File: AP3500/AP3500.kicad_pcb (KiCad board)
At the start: 4 copper layers, 105 x 105 mm, 146 parts, among them IC2 TPS23751PWPR, J1 Console, J11 Barrel_Jack, J12 Bus_PCI_Express_Mini, J9 0826-1X1T-GH-F, Q1 FDS86242, U1 TPD4EUSB30, U10 TPS563249DDCR, U11 TPS563249DDCR, U12 HMHA2801AR2, U13 TPS563249DDCR, U2 TPD4EUSB30, U3 SN74LVC07AD, U5 74LVC1G07SE-7, U6 TL431AIDBVR

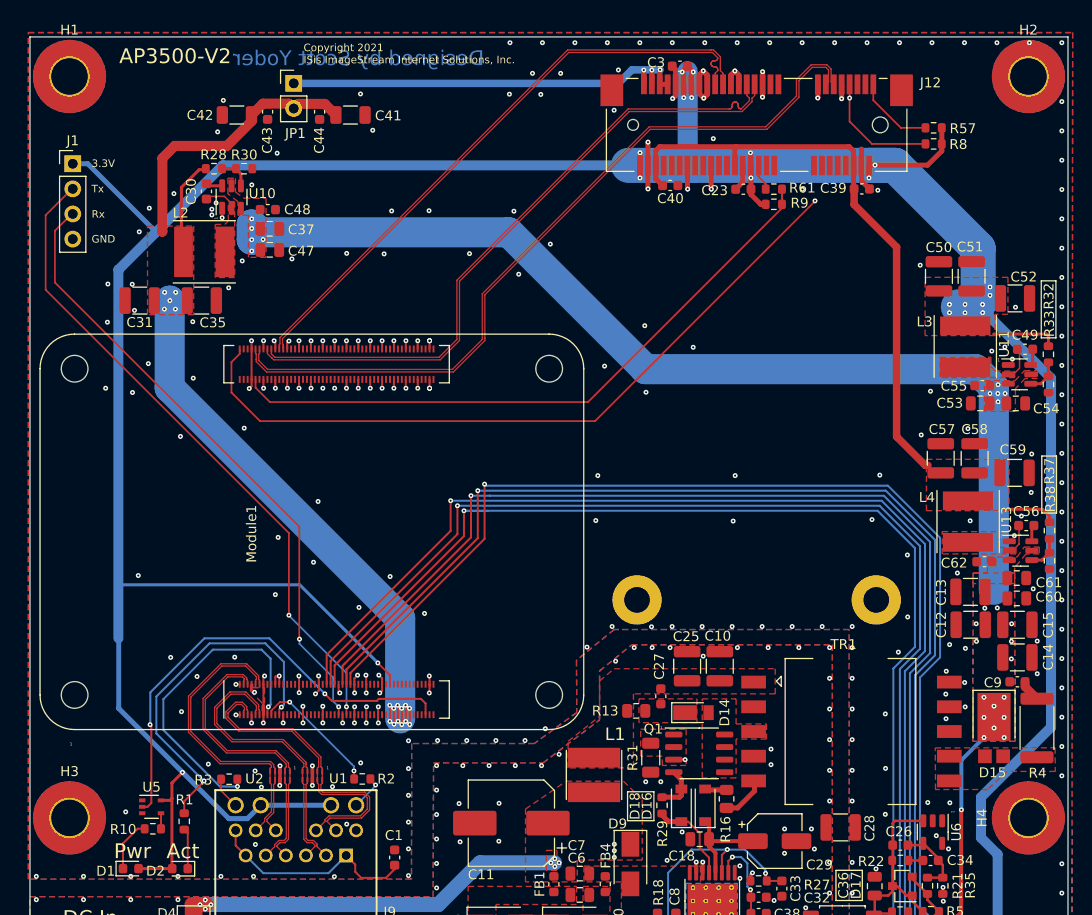
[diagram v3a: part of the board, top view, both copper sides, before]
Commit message: Add new single polarity aperture coupled 4x4 antenna. RasPiCNM4Connector test Gerbers for PCBWay Cleanups and optimixations for AP3500
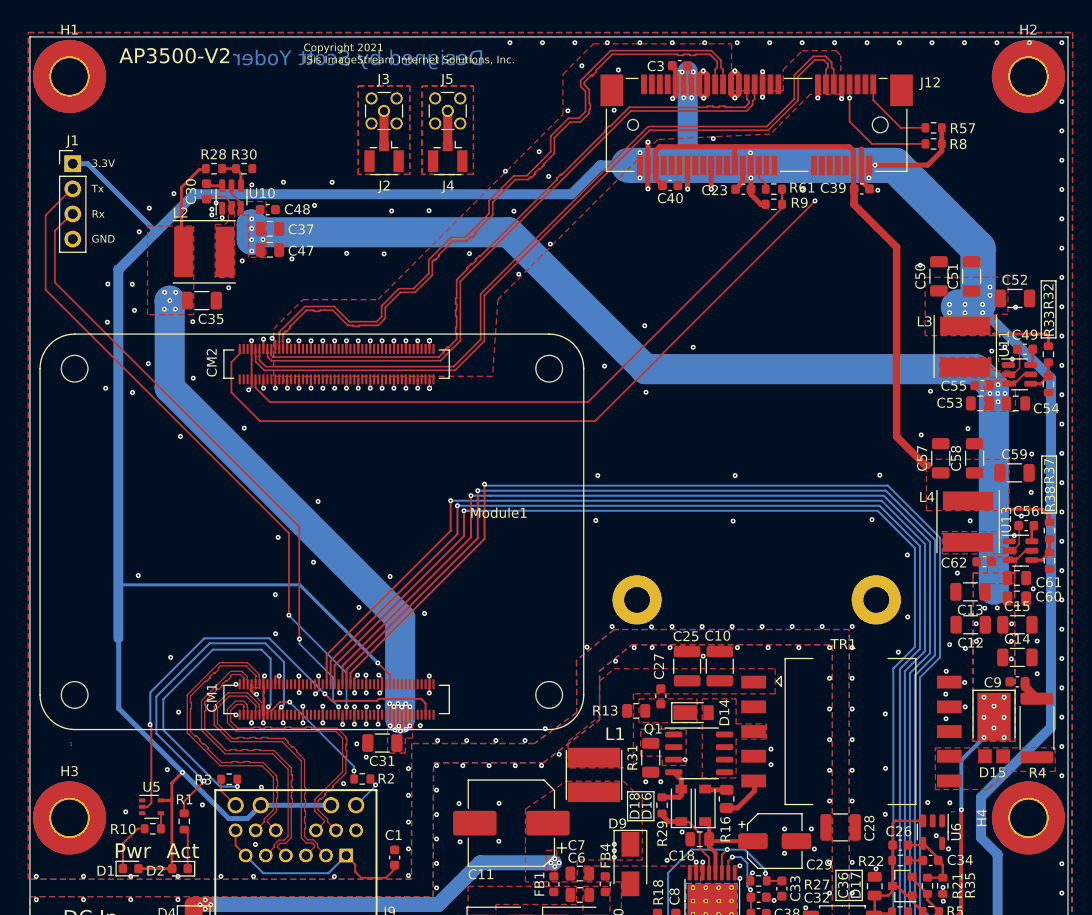
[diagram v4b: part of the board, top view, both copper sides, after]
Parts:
- removed C41, C42: 47u 10v, Capacitor_SMD:C_1206_3216Metric
- removed C43, C44: .1u 25v, Capacitor_SMD:C_0603_1608Metric
- removed JP1: Jumper_2_Open, Connector_PinHeader_2.54mm:PinHeader_1x02_P2.54mm_Vertical
- removed U1, U2: TPD4EUSB30, Scott:USON-10_2.51x1.0mm_P0.5mm
- added CM1: RaspberryPiCM4Hirose, AP3000:Hirose-DF40C-100DS-0.4V, F.Cu at (31.0, 67.0)
- added CM2: RaspberryPiCM4Hirose, AP3000:Hirose-DF40C-100DS-0.4V, F.Cu at (31.0, 33.1)
- added J2: Conn_Coaxial, Connector_Coaxial:U.FL_Hirose_U.FL-R-SMT-1_Vertical, F.Cu at (35.8, 12.1)
- added J3: Conn_Coaxial, Connector_Coaxial:MMCX_Molex_73415-1471_Vertical, F.Cu at (35.8, 7.49)
- added J4: Conn_Coaxial, Connector_Coaxial:U.FL_Hirose_U.FL-R-SMT-1_Vertical, F.Cu at (42.3, 12.1)
- added J5: Conn_Coaxial, Connector_Coaxial:MMCX_Molex_73415-1471_Vertical, F.Cu at (42.3, 7.49)
- C1: value 100n 16v -> 100n 50v
- C12, C13, C14, C15, C31, C35, C50, C51, C52, C57, C58, C59: footprint Capacitor_SMD:C_1210_3225Metric -> Capacitor_SMD:C_1206_3216Metric
- C18: value 1uF 25V -> 1u 25v
- C23, C3, C39, C40: value .1u 25v -> 100n 50v
- Module1: footprint AP3500:Raspberry-Pi-4-Compute-Module -> AP3000:Raspberry-Pi-4-Compute-Module
- R61: value 0 1% -> 0R 1%
- moved C31 51.0 mm to (35.6, 71.4)
- moved Module1 21.5 mm to (31.0, 67.0)
- moved C3 0.05 mm to (65.7, 2.91)
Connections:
- IC2 pad 7: no_connect_(IC2-Pad7) -> unconnected-(IC2-Pad7)
- J12 pad 10: no_connect_(J12-Pad10) -> unconnected-(J12-Pad10)
- J12 pad 12: no_connect_(J12-Pad12) -> unconnected-(J12-Pad12)
- J12 pad 14: no_connect_(J12-Pad14) -> unconnected-(J12-Pad14)
- J12 pad 16: no_connect_(J12-Pad16) -> unconnected-(J12-Pad16)
- J12 pad 17: no_connect_(J12-Pad17) -> unconnected-(J12-Pad17)
- J12 pad 19: no_connect_(J12-Pad19) -> unconnected-(J12-Pad19)
- J12 pad 20: no_connect_(J12-Pad20) -> unconnected-(J12-Pad20)
- J12 pad 3: no_connect_(J12-Pad3) -> unconnected-(J12-Pad3)
- J12 pad 30: no_connect_(J12-Pad30) -> unconnected-(J12-Pad30)
- J12 pad 32: no_connect_(J12-Pad32) -> unconnected-(J12-Pad32)
- J12 pad 36: no_connect_(J12-Pad36) -> unconnected-(J12-Pad36)
- J12 pad 38: no_connect_(J12-Pad38) -> unconnected-(J12-Pad38)
- J12 pad 42: no_connect_(J12-Pad42) -> unconnected-(J12-Pad42)
- J12 pad 44: no_connect_(J12-Pad44) -> unconnected-(J12-Pad44)
- J12 pad 45: Net-(J12-Pad45) -> unconnected-(J12-Pad45)
- J12 pad 46: no_connect_(J12-Pad46) -> unconnected-(J12-Pad46)
- J12 pad 47: Net-(J12-Pad45) -> unconnected-(J12-Pad47)
- J12 pad 49: Net-(J12-Pad45) -> unconnected-(J12-Pad49)
- J12 pad 5: no_connect_(J12-Pad5) -> unconnected-(J12-Pad5)
- J12 pad 51: Net-(J12-Pad45) -> unconnected-(J12-Pad51)
- J12 pad 8: no_connect_(J12-Pad8) -> unconnected-(J12-Pad8)
- Module1 pad 100: no_connect_(Module1-Pad100) -> unconnected-(Module1-Pad100)
- Module1 pad 101: no_connect_(Module1-Pad101) -> unconnected-(Module1-Pad101)
- Module1 pad 103: no_connect_(Module1-Pad103) -> unconnected-(Module1-Pad103)
- Module1 pad 104: no_connect_(Module1-Pad104) -> unconnected-(Module1-Pad104)
- Module1 pad 105: no_connect_(Module1-Pad105) -> unconnected-(Module1-Pad105)
- Module1 pad 106: no_connect_(Module1-Pad106) -> unconnected-(Module1-Pad106)
- Module1 pad 111: no_connect_(Module1-Pad111) -> unconnected-(Module1-Pad111)
- Module1 pad 115: no_connect_(Module1-Pad115) -> unconnected-(Module1-Pad115)
- Module1 pad 117: no_connect_(Module1-Pad117) -> unconnected-(Module1-Pad117)
- Module1 pad 121: no_connect_(Module1-Pad121) -> unconnected-(Module1-Pad121)
- Module1 pad 123: no_connect_(Module1-Pad123) -> unconnected-(Module1-Pad123)
- Module1 pad 127: no_connect_(Module1-Pad127) -> unconnected-(Module1-Pad127)
- Module1 pad 128: no_connect_(Module1-Pad128) -> unconnected-(Module1-Pad128)
- Module1 pad 129: no_connect_(Module1-Pad129) -> unconnected-(Module1-Pad129)
- Module1 pad 130: no_connect_(Module1-Pad130) -> unconnected-(Module1-Pad130)
- Module1 pad 133: no_connect_(Module1-Pad133) -> unconnected-(Module1-Pad133)
- Module1 pad 134: no_connect_(Module1-Pad134) -> unconnected-(Module1-Pad134)
- Module1 pad 135: no_connect_(Module1-Pad135) -> unconnected-(Module1-Pad135)
- Module1 pad 136: no_connect_(Module1-Pad136) -> unconnected-(Module1-Pad136)
- Module1 pad 139: no_connect_(Module1-Pad139) -> unconnected-(Module1-Pad139)
- Module1 pad 140: no_connect_(Module1-Pad140) -> unconnected-(Module1-Pad140)
- Module1 pad 141: no_connect_(Module1-Pad141) -> unconnected-(Module1-Pad141)
- Module1 pad 142: no_connect_(Module1-Pad142) -> unconnected-(Module1-Pad142)
- Module1 pad 143: no_connect_(Module1-Pad143) -> unconnected-(Module1-Pad143)
- Module1 pad 145: no_connect_(Module1-Pad145) -> unconnected-(Module1-Pad145)
- Module1 pad 146: no_connect_(Module1-Pad146) -> unconnected-(Module1-Pad146)
- Module1 pad 147: no_connect_(Module1-Pad147) -> unconnected-(Module1-Pad147)
- Module1 pad 148: no_connect_(Module1-Pad148) -> unconnected-(Module1-Pad148)
- Module1 pad 149: no_connect_(Module1-Pad149) -> unconnected-(Module1-Pad149)
- Module1 pad 151: no_connect_(Module1-Pad151) -> unconnected-(Module1-Pad151)
- Module1 pad 152: no_connect_(Module1-Pad152) -> unconnected-(Module1-Pad152)
- Module1 pad 153: no_connect_(Module1-Pad153) -> unconnected-(Module1-Pad153)
- Module1 pad 154: no_connect_(Module1-Pad154) -> unconnected-(Module1-Pad154)
- Module1 pad 157: no_connect_(Module1-Pad157) -> unconnected-(Module1-Pad157)
- Module1 pad 158: no_connect_(Module1-Pad158) -> unconnected-(Module1-Pad158)
- Module1 pad 159: no_connect_(Module1-Pad159) -> unconnected-(Module1-Pad159)
- Module1 pad 16: no_connect_(Module1-Pad16) -> unconnected-(Module1-Pad16)
- Module1 pad 160: no_connect_(Module1-Pad160) -> unconnected-(Module1-Pad160)
- Module1 pad 163: no_connect_(Module1-Pad163) -> unconnected-(Module1-Pad163)
- Module1 pad 164: no_connect_(Module1-Pad164) -> unconnected-(Module1-Pad164)
- Module1 pad 165: no_connect_(Module1-Pad165) -> unconnected-(Module1-Pad165)
- Module1 pad 166: no_connect_(Module1-Pad166) -> unconnected-(Module1-Pad166)
- Module1 pad 169: no_connect_(Module1-Pad169) -> unconnected-(Module1-Pad169)
- Module1 pad 170: no_connect_(Module1-Pad170) -> unconnected-(Module1-Pad170)
- Module1 pad 171: no_connect_(Module1-Pad171) -> unconnected-(Module1-Pad171)
- Module1 pad 172: no_connect_(Module1-Pad172) -> unconnected-(Module1-Pad172)
- Module1 pad 175: no_connect_(Module1-Pad175) -> unconnected-(Module1-Pad175)
- Module1 pad 176: no_connect_(Module1-Pad176) -> unconnected-(Module1-Pad176)
- Module1 pad 177: no_connect_(Module1-Pad177) -> unconnected-(Module1-Pad177)
- Module1 pad 178: no_connect_(Module1-Pad178) -> unconnected-(Module1-Pad178)
- Module1 pad 18: no_connect_(Module1-Pad18) -> unconnected-(Module1-Pad18)
- Module1 pad 181: no_connect_(Module1-Pad181) -> unconnected-(Module1-Pad181)
- Module1 pad 182: no_connect_(Module1-Pad182) -> unconnected-(Module1-Pad182)
- Module1 pad 183: no_connect_(Module1-Pad183) -> unconnected-(Module1-Pad183)
- Module1 pad 184: no_connect_(Module1-Pad184) -> unconnected-(Module1-Pad184)
- Module1 pad 187: no_connect_(Module1-Pad187) -> unconnected-(Module1-Pad187)
- Module1 pad 188: no_connect_(Module1-Pad188) -> unconnected-(Module1-Pad188)
- Module1 pad 189: no_connect_(Module1-Pad189) -> unconnected-(Module1-Pad189)
- Module1 pad 19: no_connect_(Module1-Pad19) -> unconnected-(Module1-Pad19)
- Module1 pad 190: no_connect_(Module1-Pad190) -> unconnected-(Module1-Pad190)
- Module1 pad 193: no_connect_(Module1-Pad193) -> unconnected-(Module1-Pad193)
- Module1 pad 194: no_connect_(Module1-Pad194) -> unconnected-(Module1-Pad194)
- Module1 pad 195: no_connect_(Module1-Pad195) -> unconnected-(Module1-Pad195)
- Module1 pad 196: no_connect_(Module1-Pad196) -> unconnected-(Module1-Pad196)
- Module1 pad 199: no_connect_(Module1-Pad199) -> unconnected-(Module1-Pad199)
- Module1 pad 200: no_connect_(Module1-Pad200) -> unconnected-(Module1-Pad200)
- Module1 pad 35: no_connect_(Module1-Pad35) -> unconnected-(Module1-Pad35)
- Module1 pad 36: no_connect_(Module1-Pad36) -> unconnected-(Module1-Pad36)
- Module1 pad 57: no_connect_(Module1-Pad57) -> unconnected-(Module1-Pad57)
- Module1 pad 61: no_connect_(Module1-Pad61) -> unconnected-(Module1-Pad61)
- Module1 pad 62: no_connect_(Module1-Pad62) -> unconnected-(Module1-Pad62)
- Module1 pad 63: no_connect_(Module1-Pad63) -> unconnected-(Module1-Pad63)
- Module1 pad 64: no_connect_(Module1-Pad64) -> unconnected-(Module1-Pad64)
- Module1 pad 67: no_connect_(Module1-Pad67) -> unconnected-(Module1-Pad67)
- Module1 pad 68: no_connect_(Module1-Pad68) -> unconnected-(Module1-Pad68)
- Module1 pad 69: no_connect_(Module1-Pad69) -> unconnected-(Module1-Pad69)
- Module1 pad 70: no_connect_(Module1-Pad70) -> unconnected-(Module1-Pad70)
- Module1 pad 72: no_connect_(Module1-Pad72) -> unconnected-(Module1-Pad72)
- Module1 pad 73: no_connect_(Module1-Pad73) -> unconnected-(Module1-Pad73)
- Module1 pad 75: no_connect_(Module1-Pad75) -> unconnected-(Module1-Pad75)
- Module1 pad 76: no_connect_(Module1-Pad76) -> unconnected-(Module1-Pad76)
- Module1 pad 80: no_connect_(Module1-Pad80) -> unconnected-(Module1-Pad80)
- Module1 pad 82: no_connect_(Module1-Pad82) -> unconnected-(Module1-Pad82)
- Module1 pad 84: no_connect_(Module1-Pad84) -> unconnected-(Module1-Pad84)
- Module1 pad 86: no_connect_(Module1-Pad86) -> unconnected-(Module1-Pad86)
- Module1 pad 88: no_connect_(Module1-Pad88) -> unconnected-(Module1-Pad88)
- Module1 pad 89: no_connect_(Module1-Pad89) -> unconnected-(Module1-Pad89)
- Module1 pad 90: no_connect_(Module1-Pad90) -> unconnected-(Module1-Pad90)
- Module1 pad 91: no_connect_(Module1-Pad91) -> unconnected-(Module1-Pad91)
- Module1 pad 92: no_connect_(Module1-Pad92) -> unconnected-(Module1-Pad92)
- Module1 pad 93: no_connect_(Module1-Pad93) -> unconnected-(Module1-Pad93)
- Module1 pad 94: no_connect_(Module1-Pad94) -> unconnected-(Module1-Pad94)
- Module1 pad 96: no_connect_(Module1-Pad96) -> unconnected-(Module1-Pad96)
- Module1 pad 97: no_connect_(Module1-Pad97) -> unconnected-(Module1-Pad97)
- Module1 pad 99: no_connect_(Module1-Pad99) -> unconnected-(Module1-Pad99)
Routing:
- net Net-(J12-Pad45): track 43.7 -> 0.00 mm, vias 3 -> 0
- net /+5v: track 100.3 -> 75.8 mm
- net /+12v: track 125.4 -> 133.4 mm
- net /RF_SIG1: track 0.00 -> 7.10 mm
- net /CM4_HighSpeed/PCIE_TX_P: track 61.0 -> 68.0 mm
- net /CM4_HighSpeed/PCIE_TX_N: track 61.0 -> 68.0 mm
- net /CM4_GPIO ( Ethernet, GPIO, SDCARD)/E0_TRD3_N: track 31.3 -> 28.4 mm
- net /CM4_GPIO ( Ethernet, GPIO, SDCARD)/E0_TRD3_P: track 30.5 -> 28.2 mm
- net GND: track 105.0 -> 106.3 mm, vias 312 -> 307
- net /CM4_HighSpeed/PCIE_CLK_P: track 77.8 -> 79.0 mm
- net /CM4_HighSpeed/PCIE_CLK_N: track 77.8 -> 79.0 mm
- net /CM4_GPIO ( Ethernet, GPIO, SDCARD)/E0_TRD1_P: track 29.0 -> 30.1 mm
- net /CM4_GPIO ( Ethernet, GPIO, SDCARD)/E0_TRD0_N: track 29.9 -> 30.6 mm
- net /CM4_GPIO ( Ethernet, GPIO, SDCARD)/E0_TRD2_N: track 28.9 -> 29.5 mm
- added copper zone on F.Cu, net /RF_GND1

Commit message: Rework AP3500
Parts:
- TR1: footprint Scott:Transformer_TNK_TSE265 -> Scott:Transformer_Dual_TNK_TSE265_Wurth
- moved J2 3.00 mm to (34.7, 9.32)
- moved J4 2.77 mm to (42.2, 9.32)
- moved J3 2.06 mm to (34.7, 5.78)
- moved J5 1.71 mm to (42.3, 5.78)
- moved TR1 1.06 mm to (83.3, 70.2)
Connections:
- J4 pad 1: /RF_SIG1 -> /RF_SIG2
- J4 pad 2: /RF_GND1 -> /RF_GND2
- J5 pad 1: /RF_SIG1 -> /RF_SIG2
- J5 pad 2: /RF_GND1 -> /RF_GND2
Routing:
- net /RF_SIG1: track 7.10 -> 2.49 mm
- net /RF_SIG2: track 0.00 -> 2.49 mm
- net /CM4_HighSpeed/PCIE_nRST: track 64.7 -> 65.3 mm
- net /CM4_GPIO ( Ethernet, GPIO, SDCARD)/E0_LEDY: track 13.1 -> 13.6 mm
- net GNDPWR: vias 86 -> 87
- net GND: vias 307 -> 311
- added copper zone on F.Cu, net /RF_GND2

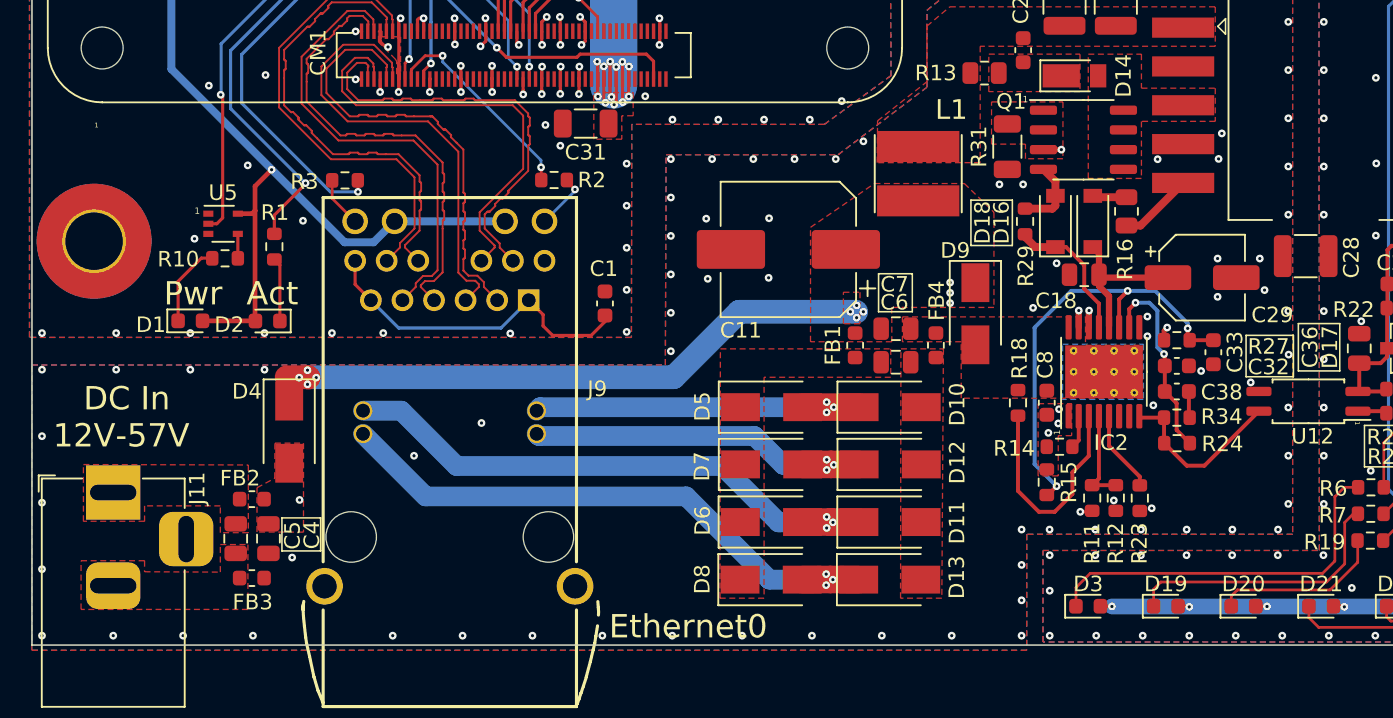
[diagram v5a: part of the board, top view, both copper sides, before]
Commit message: Updates for JLCPCB components actually in stock at this time
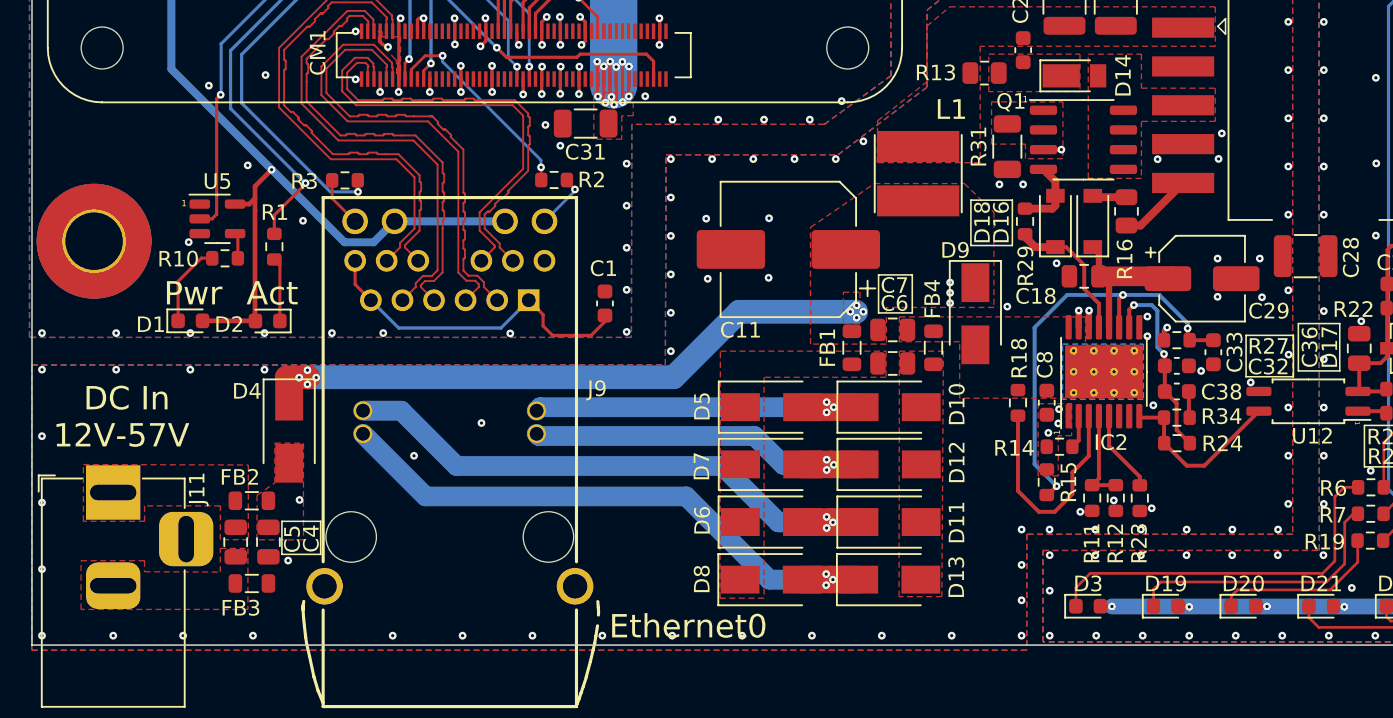
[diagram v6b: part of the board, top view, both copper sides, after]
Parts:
- C29: footprint Capacitor_SMD:CP_Elec_5x5.8 -> Capacitor_SMD:CP_Elec_5x5.4
- FB1, FB2, FB3, FB4: footprint Inductor_SMD:L_0603_1608Metric -> Inductor_SMD:L_0805_2012Metric
- U5: footprint Package_TO_SOT_SMD:SOT-353_SC-70-5 -> Package_TO_SOT_SMD:SOT-23-5
- moved U5 0.48 mm to (11.9, 77.6)
- moved FB3 0.35 mm to (14.2, 101.0)
- moved FB1 0.26 mm to (52.8, 85.9)
- moved C4 0.22 mm to (15.2, 98.4)
- moved C5 0.22 mm to (13.1, 98.4)
- moved FB4 0.22 mm to (58.0, 85.9)
- moved C6 0.22 mm to (55.4, 86.9)
- moved C7 0.22 mm to (55.4, 84.7)
- moved C18 0.10 mm to (67.7, 81.3)
- moved FB2 0.10 mm to (14.2, 95.7)
- moved C29 0.07 mm to (75.3, 81.4)
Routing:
- net Net-(C33-Pad1): track 28.6 -> 28.0 mm

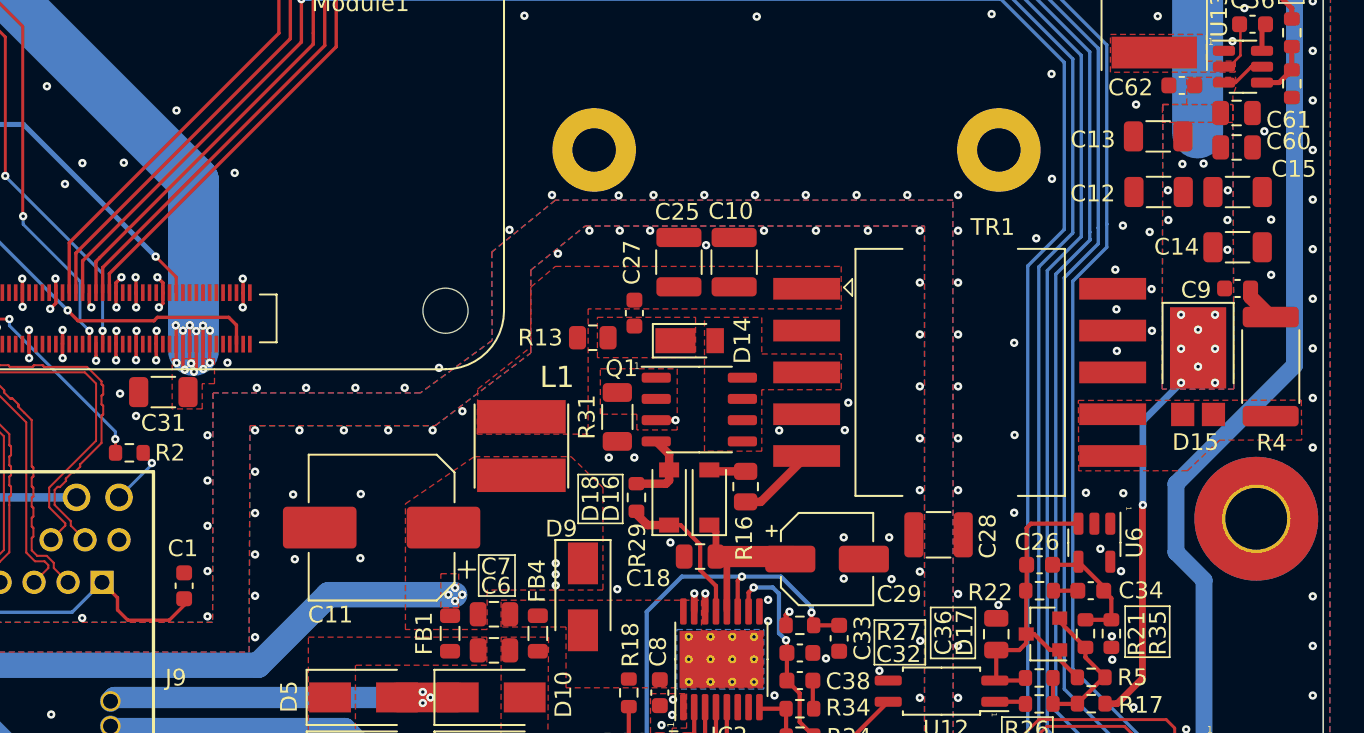
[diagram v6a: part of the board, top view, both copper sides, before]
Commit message: Update AP3500 with new Wurth footprint - needed rerouted. Fix the gigabit ethernet problem with pair 4 center tap to ground instead of through cap.
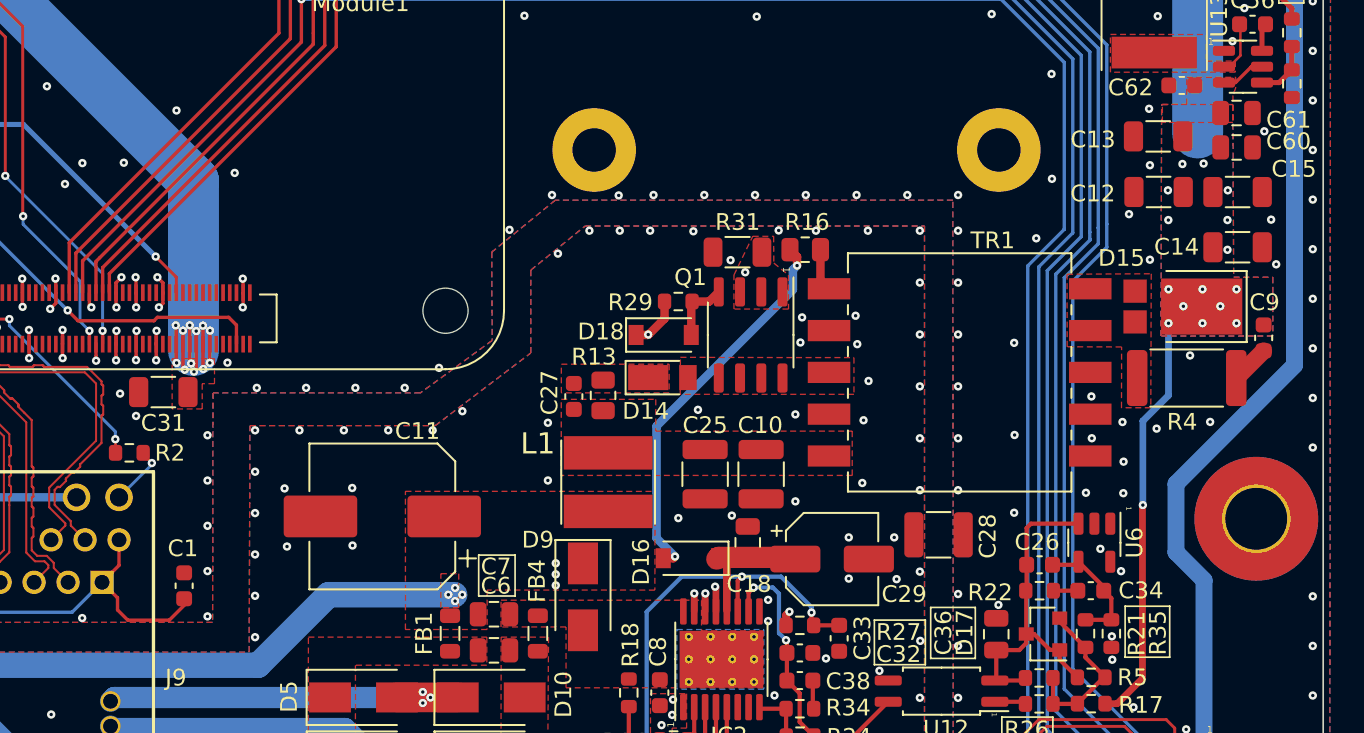
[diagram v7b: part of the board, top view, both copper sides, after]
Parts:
- TR1: footprint Scott:Transformer_Dual_TNK_TSE265_Wurth -> Scott:Transformer_EP13
- moved R16 14.6 mm to (74.0, 62.9), turned to 0 degrees
- moved C10 12.8 mm to (71.4, 76.3), turned to -90 degrees
- moved C25 12.8 mm to (68.0, 76.3), turned to -90 degrees
- moved R31 12.2 mm to (70.0, 63.1), turned to 0 degrees
- moved R29 12.0 mm to (66.4, 66.0), turned to 0 degrees
- moved D18 9.72 mm to (65.6, 68.0), turned to 0 degrees
- moved C27 6.16 mm to (60.2, 71.7), turned to 90 degrees
- moved L1 5.61 mm to (62.2, 76.8)
- moved Q1 5.41 mm to (70.8, 68.0), turned to -90 degrees
- moved R4 5.07 mm to (96.8, 70.6), turned to 180 degrees
- moved D16 3.80 mm to (67.2, 81.4), turned to 180 degrees
- moved D15 3.70 mm to (96.6, 66.3), turned to 180 degrees
- moved R13 3.50 mm to (61.9, 71.6), turned to 90 degrees
- moved C9 3.34 mm to (101.4, 68.2), turned to 90 degrees
- moved C18 2.97 mm to (70.6, 80.4), turned to 90 degrees
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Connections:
- J9 pad 7: GND -> Net-(C1-Pad1)
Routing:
- net Net-(D16-Pad2): track 2.24 -> 23.2 mm, vias 0 -> 2
- net Net-(D18-Pad1): track 9.12 -> 21.4 mm, vias 0 -> 2
- net Net-(Q1-Pad1): track 16.3 -> 22.3 mm
- net /+12v: track 133.4 -> 136.7 mm
- net Net-(C1-Pad1): track 21.6 -> 24.6 mm
- net Net-(R16-Pad2): track 4.75 -> 2.55 mm
- net /PoE/VC: track 10.4 -> 8.47 mm
- net Net-(D18-Pad2): track 4.69 -> 3.85 mm
- net GNDPWR: vias 87 -> 95
- net GND: vias 311 -> 314
